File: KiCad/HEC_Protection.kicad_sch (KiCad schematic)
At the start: 19 parts, among them U10 74LS32, U11 74LS00, U11 74LS32, U12 74LS04, U17 74LS74, U18 74LS138, U18 74LS74, U19 74LS30, U22 74LS02, U23 74LS74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

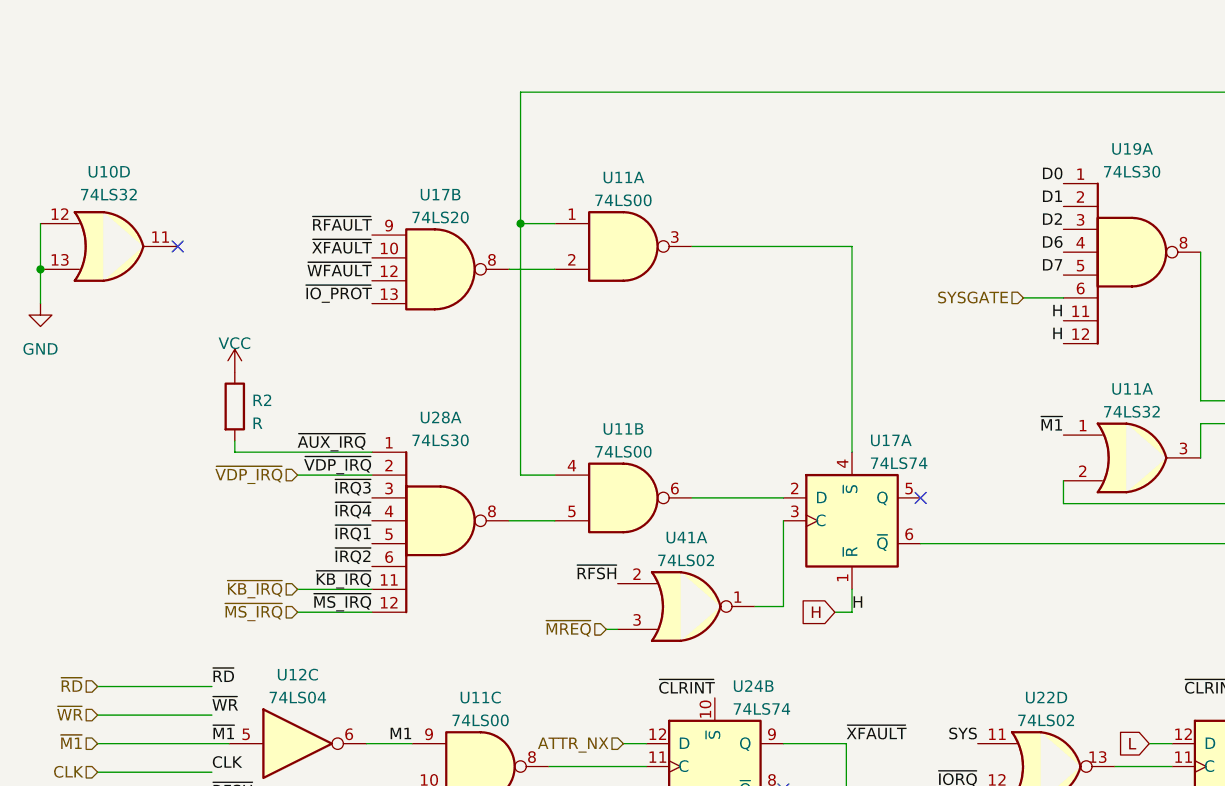
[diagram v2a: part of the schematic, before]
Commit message: New bus symbol
Updated bus symbol and footprint to simplify PCB layout.
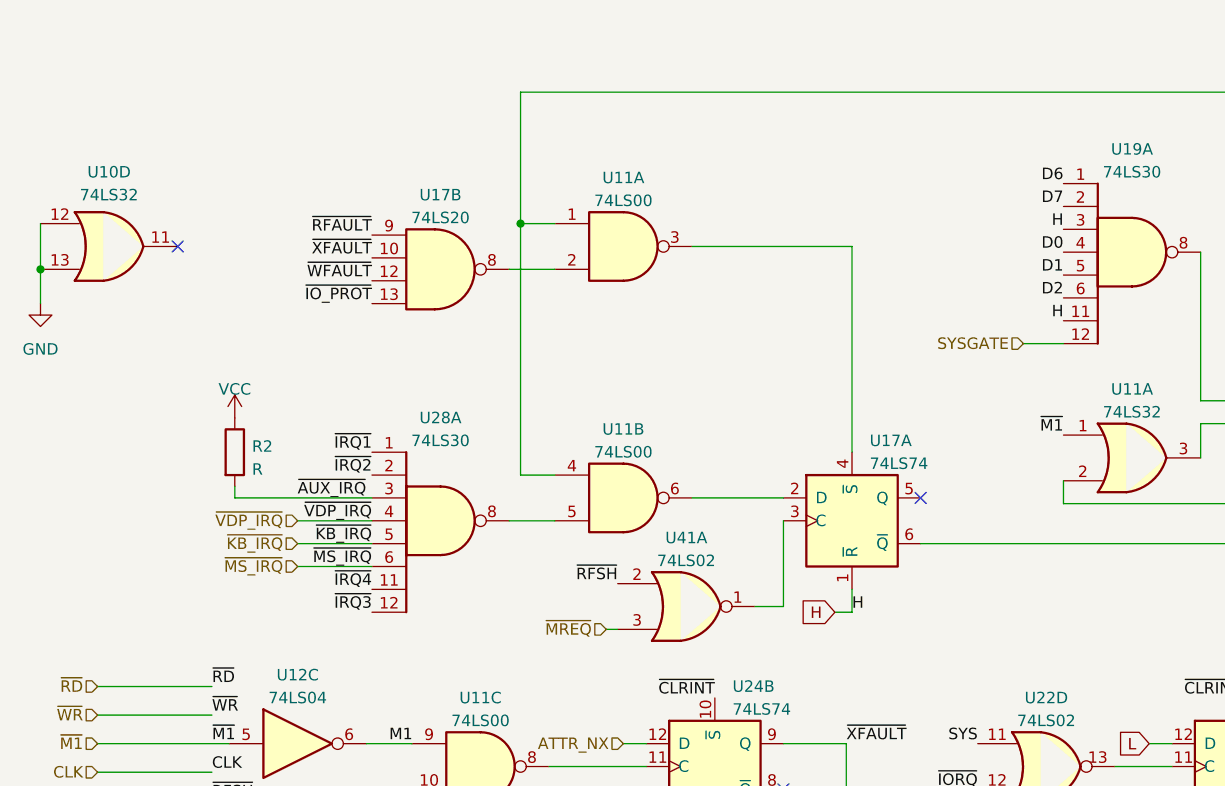
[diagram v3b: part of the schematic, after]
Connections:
- net D0: now also U19.4; no longer U19.1
- net D1: now also U19.5; no longer U19.2
- net D2: now also U19.6; no longer U19.3
- net D6: now also U19.1; no longer U19.4
- net D7: now also U19.2; no longer U19.5
- net H: now also U19.3; no longer U19.12
- net SYSGATE: now also U19.12; no longer U19.6
- net ~{AUX_IRQ}: now also U28.3; no longer U28.1
- net ~{IRQ1}: now also U28.1; no longer U28.5
- net ~{IRQ2}: now also U28.2; no longer U28.6
- net ~{IRQ3}: now also U28.12; no longer U28.3
- net ~{IRQ4}: now also U28.11; no longer U28.4
- net ~{KB_IRQ}: now also U28.5; no longer U28.11
- net ~{MS_IRQ}: now also U28.6; no longer U28.12
- net ~{VDP_IRQ}: now also U28.4; no longer U28.2
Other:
- moved on the sheet: R2
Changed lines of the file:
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@@
     (stroke (width 0) (type default))
   )
-  (wire (pts (xy 133.985 41.91) (xy 138.43 41.91))
-    (stroke (width 0) (type default))
-  )
-  (wire (pts (xy 53.34 76.835) (xy 61.595 76.835))
+  (wire (pts (xy 133.985 46.99) (xy 138.43 46.99))
+    (stroke (width 0) (type default))
+  )
+  (wire (pts (xy 53.34 71.755) (xy 61.595 71.755))
     (stroke (width 0) (type default))
   )
@@
     (stroke (width 0) (type default))
   )
-  (wire (pts (xy 46.355 57.785) (xy 46.355 59.055))
+  (wire (pts (xy 46.355 62.865) (xy 46.355 64.135))
     (stroke (width 0) (type default))
   )
@@
     (stroke (width 0) (type default))
   )
-  (wire (pts (xy 53.34 61.595) (xy 61.595 61.595))
+  (wire (pts (xy 53.34 66.675) (xy 61.595 66.675))
     (stroke (width 0) (type default))
   )
@@
     (stroke (width 0) (type default))
   )
-  (wire (pts (xy 46.355 59.055) (xy 61.595 59.055))
+  (wire (pts (xy 46.355 64.135) (xy 61.595 64.135))
     (stroke (width 0) (type default))
   )
@@
     (stroke (width 0) (type default))
   )
-  (wire (pts (xy 53.34 74.295) (xy 61.595 74.295))
+  (wire (pts (xy 53.34 69.215) (xy 61.595 69.215))
     (stroke (width 0) (type default))
   )
@@
     (effects (font (size 1.27 1.27)) (justify right bottom))
   )
-  (label "~{IRQ2}" (at 61.595 71.755 180) (fields_autoplaced)
+  (label "~{IRQ2}" (at 61.595 61.595 180) (fields_autoplaced)
     (effects (font (size 1.27 1.27)) (justify right bottom))
   )
@@
     (effects (font (size 1.27 1.27)) (justify left bottom))
   )
-  (label "D1" (at 138.43 31.75 180) (fields_autoplaced)
-    (effects (font (size 1.27 1.27)) (justify right bottom))
-  )
-  (label "~{VDP_IRQ}" (at 61.595 61.595 180) (fields_autoplaced)
+  (label "D1" (at 138.43 39.37 180) (fields_autoplaced)
+    (effects (font (size 1.27 1.27)) (justify right bottom))
+  )
+  (label "~{VDP_IRQ}" (at 61.595 66.675 180) (fields_autoplaced)
     (effects (font (size 1.27 1.27)) (justify right bottom))
   )
@@
     (effects (font (size 1.27 1.27)) (justify left bottom))
   )
-  (label "D0" (at 138.43 29.21 180) (fields_autoplaced)
+  (label "D0" (at 138.43 36.83 180) (fields_autoplaced)
     (effects (font (size 1.27 1.27)) (justify right bottom))
   )
@@
     (effects (font (size 1.27 1.27)) (justify left bottom))
   )
-  (label "~{IRQ3}" (at 61.595 64.135 180) (fields_autoplaced)
+  (label "~{IRQ3}" (at 61.595 76.835 180) (fields_autoplaced)
     (effects (font (size 1.27 1.27)) (justify right bottom))
   )
@@
     (effects (font (size 1.27 1.27)) (justify left bottom))
   )
-  (label "H" (at 138.43 46.99 180) (fields_autoplaced)
+  (label "H" (at 138.43 34.29 180) (fields_autoplaced)
     (effects (font (size 1.27 1.27)) (justify right bottom))
   )
@@
     (effects (font (size 1.27 1.27)) (justify left bottom))
   )
-  (label "D2" (at 138.43 34.29 180) (fields_autoplaced)
+  (label "D2" (at 138.43 41.91 180) (fields_autoplaced)
     (effects (font (size 1.27 1.27)) (justify right bottom))
   )
@@
     (effects (font (size 1.27 1.27)) (justify right bottom))
   )
-  (label "~{AUX_IRQ}" (at 60.96 59.055 180) (fields_autoplaced)
+  (label "~{AUX_IRQ}" (at 60.96 64.135 180) (fields_autoplaced)
     (effects (font (size 1.27 1.27)) (justify right bottom))
   )
@@
     (effects (font (size 1.27 1.27)) (justify right bottom))
   )
-  (label "D7" (at 138.43 39.37 180) (fields_autoplaced)
+  (label "D7" (at 138.43 31.75 180) (fields_autoplaced)
     (effects (font (size 1.27 1.27)) (justify right bottom))
   )
@@
     (effects (font (size 1.27 1.27)) (justify left bottom))
   )
-  (label "~{KB_IRQ}" (at 61.595 74.295 180) (fields_autoplaced)
+  (label "~{KB_IRQ}" (at 61.595 69.215 180) (fields_autoplaced)
     (effects (font (size 1.27 1.27)) (justify right bottom))
   )
@@
     (effects (font (size 1.27 1.27)) (justify right bottom))
   )
-  (label "D6" (at 138.43 36.83 180) (fields_autoplaced)
+  (label "D6" (at 138.43 29.21 180) (fields_autoplaced)
     (effects (font (size 1.27 1.27)) (justify right bottom))
   )
@@
     (effects (font (size 1.27 1.27)) (justify right bottom))
   )
-  (label "~{IRQ1}" (at 61.595 69.215 180) (fields_autoplaced)
+  (label "~{IRQ1}" (at 61.595 59.055 180) (fields_autoplaced)
     (effects (font (size 1.27 1.27)) (justify right bottom))
   )
@@
     (effects (font (size 1.27 1.27)) (justify right bottom))
   )
-  (label "~{MS_IRQ}" (at 61.595 76.835 180) (fields_autoplaced)
+  (label "~{MS_IRQ}" (at 61.595 71.755 180) (fields_autoplaced)
     (effects (font (size 1.27 1.27)) (justify right bottom))
   )
@@
     (effects (font (size 1.27 1.27)) (justify left bottom))
   )
-  (label "~{IRQ4}" (at 61.595 66.675 180) (fields_autoplaced)
+  (label "~{IRQ4}" (at 61.595 74.295 180) (fields_autoplaced)
     (effects (font (size 1.27 1.27)) (justify right bottom))
   )
@@
     (effects (font (size 1.27 1.27)) (justify right))
   )
-  (hierarchical_label "~{KB_IRQ}" (shape input) (at 53.34 74.295 180) (fields_autoplaced)
+  (hierarchical_label "~{KB_IRQ}" (shape input) (at 53.34 69.215 180) (fields_autoplaced)
     (effects (font (size 1.27 1.27)) (justify right))
   )
@@
     (effects (font (size 1.27 1.27)) (justify right))
   )
-  (hierarchical_label "SYSGATE" (shape input) (at 133.985 41.91 180) (fields_autoplaced)
+  (hierarchical_label "SYSGATE" (shape input) (at 133.985 46.99 180) (fields_autoplaced)
     (effects (font (size 1.27 1.27)) (justify right))
   )
@@
     (effects (font (size 1.27 1.27)) (justify left))
   )
-  (hierarchical_label "~{VDP_IRQ}" (shape input) (at 53.34 61.595 180) (fields_autoplaced)
+  (hierarchical_label "~{VDP_IRQ}" (shape input) (at 53.34 66.675 180) (fields_autoplaced)
     (effects (font (size 1.27 1.27)) (justify right))
   )
-  (hierarchical_label "~{MS_IRQ}" (shape input) (at 53.34 76.835 180) (fields_autoplaced)
+  (hierarchical_label "~{MS_IRQ}" (shape input) (at 53.34 71.755 180) (fields_autoplaced)
     (effects (font (size 1.27 1.27)) (justify right))
   )
@@
     )
   )
-  (symbol (lib_id "power:VCC") (at 46.355 50.165 0) (unit 1)
-    (in_bom yes) (on_board yes) (dnp no) (fields_autoplaced)
-    (property "Reference" "#PWR0111" (at 46.355 53.975 0)
-      (effects (font (size 1.27 1.27)) hide)
-    )
-    (property "Value" "VCC" (at 46.355 46.99 0)
-      (effects (font (size 1.27 1.27)))
-    )
-    (property "Footprint" "" (at 46.355 50.165 0)
-      (effects (font (size 1.27 1.27)) hide)
-    )
-    (property "Datasheet" "" (at 46.355 50.165 0)
+  (symbol (lib_id "power:VCC") (at 46.355 55.245 0) (unit 1)
+    (in_bom yes) (on_board yes) (dnp no) (fields_autoplaced)
+    (property "Reference" "#PWR0111" (at 46.355 59.055 0)
+      (effects (font (size 1.27 1.27)) hide)
+    )
+    (property "Value" "VCC" (at 46.355 52.07 0)
+      (effects (font (size 1.27 1.27)))
+    )
+    (property "Footprint" "" (at 46.355 55.245 0)
+      (effects (font (size 1.27 1.27)) hide)
+    )
+    (property "Datasheet" "" (at 46.355 55.245 0)
       (effects (font (size 1.27 1.27)) hide)
     )
@@
     )
   )
-  (symbol (lib_id "Device:R") (at 46.355 53.975 0) (unit 1)
-    (in_bom yes) (on_board yes) (dnp no) (fields_autoplaced)
-    (property "Reference" "R2" (at 48.26 53.34 0)
-      (effects (font (size 1.27 1.27)) (justify left))
-    )
-    (property "Value" "R" (at 48.26 55.88 0)
-      (effects (font (size 1.27 1.27)) (justify left))
-    )
-    (property "Footprint" "Resistor_THT:R_Axial_DIN0207_L6.3mm_D2.5mm_P7.62mm_Horizontal" (at 44.577 53.975 90)
-      (effects (font (size 1.27 1.27)) hide)
-    )
-    (property "Datasheet" "~" (at 46.355 53.975 0)
-      (effects (font (size 1.27 1.27)) hide)
-    )
+  (symbol (lib_id "Device:R") (at 46.355 59.055 0) (unit 1)
+    (in_bom yes) (on_board yes) (dnp no) (fields_autoplaced)
+    (property "Reference" "R2" (at 48.26 58.42 0)
+      (effects (font (size 1.27 1.27)) (justify left))
+    )
+    (property "Value" "R" (at 48.26 60.96 0)
+      (effects (font (size 1.27 1.27)) (justify left))
+    )
+    (property "Footprint" "Resistor_THT:R_Axial_DIN0207_L6.3mm_D2.5mm_P7.62mm_Horizontal" (at 44.577 59.055 90)
+      (effects (font (size 1.27 1.27)) hide)
+    )
+    (property "Datasheet" "~" (at 46.355 59.055 0)
+      (effects (font (size 1.27 1.27)) hide)
+    )

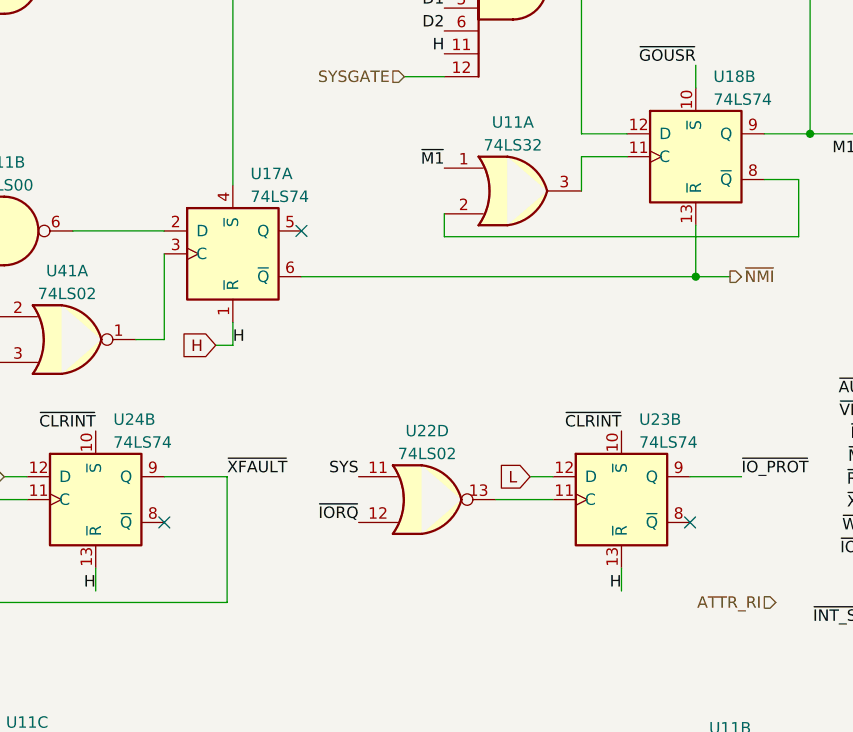
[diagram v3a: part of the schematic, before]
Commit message: Livestream routing
First routing livestream! Routed a data bus and some traces protection and memory region.
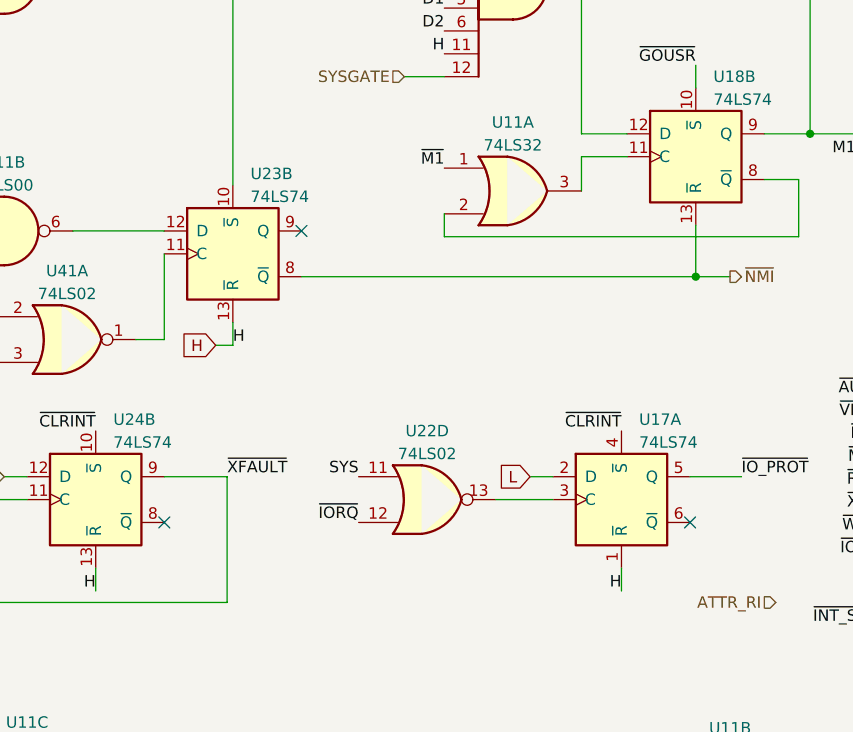
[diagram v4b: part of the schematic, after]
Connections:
- net L: now also U17.2 (D); no longer U23.12 (D)
- net ~{CLRINT}: now also U17.4 (~{S}); no longer U23.10 (~{S})
- net ~{IO_PROT}: now also U17.5 (Q); no longer U23.9 (Q)
- net ~{NMI}: now also U23.8 (~{Q}); no longer U17.6 (~{Q})
- net at U23.11 (C): now also U41.1; no longer U22.13
- net at U11.3: now also U23.10 (~{S}); no longer U17.4 (~{S})
- net at U17.3 (C): now also U22.13; no longer U41.1
- net at U11.6: now also U23.12 (D); no longer U17.2 (D)
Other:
- moved on the sheet: U17A, U23B
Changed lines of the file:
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@@
     )
   )
-  (symbol (lib_id "74xx:74LS74") (at 158.115 93.98 0) (unit 2)
-    (in_bom yes) (on_board yes) (dnp no) (fields_autoplaced)
-    (property "Reference" "U23" (at 160.0709 85.09 0)
-      (effects (font (size 1.27 1.27)) (justify left))
-    )
-    (property "Value" "74LS74" (at 160.0709 87.63 0)
-      (effects (font (size 1.27 1.27)) (justify left))
-    )
-    (property "Footprint" "Package_DIP:DIP-14_W7.62mm_Socket" (at 158.115 93.98 0)
-      (effects (font (size 1.27 1.27)) hide)
-    )
-    (property "Datasheet" "74xx/74hc_hct74.pdf" (at 158.115 93.98 0)
+  (symbol (lib_id "74xx:74LS74") (at 114.935 66.675 0) (unit 2)
+    (in_bom yes) (on_board yes) (dnp no) (fields_autoplaced)
+    (property "Reference" "U23" (at 116.8909 57.785 0)
+      (effects (font (size 1.27 1.27)) (justify left))
+    )
+    (property "Value" "74LS74" (at 116.8909 60.325 0)
+      (effects (font (size 1.27 1.27)) (justify left))
+    )
+    (property "Footprint" "Package_DIP:DIP-14_W7.62mm_Socket" (at 114.935 66.675 0)
+      (effects (font (size 1.27 1.27)) hide)
+    )
+    (property "Datasheet" "74xx/74hc_hct74.pdf" (at 114.935 66.675 0)
       (effects (font (size 1.27 1.27)) hide)
     )
@@
     )
   )
-  (symbol (lib_id "74xx:74LS74") (at 114.935 66.675 0) (unit 1)
-    (in_bom yes) (on_board yes) (dnp no) (fields_autoplaced)
-    (property "Reference" "U17" (at 116.8909 57.785 0)
-      (effects (font (size 1.27 1.27)) (justify left))
-    )
-    (property "Value" "74LS74" (at 116.8909 60.325 0)
-      (effects (font (size 1.27 1.27)) (justify left))
-    )
-    (property "Footprint" "Package_DIP:DIP-14_W7.62mm_Socket" (at 114.935 66.675 0)
-      (effects (font (size 1.27 1.27)) hide)
-    )
-    (property "Datasheet" "74xx/74hc_hct74.pdf" (at 114.935 66.675 0)
-      (effects (font (size 1.27 1.27)) hide)
-    )
+  (symbol (lib_id "74xx:74LS74") (at 158.115 93.98 0) (unit 1)
+    (in_bom yes) (on_board yes) (dnp no) (fields_autoplaced)
+    (property "Reference" "U17" (at 160.0709 85.09 0)
+      (effects (font (size 1.27 1.27)) (justify left))
+    )
+    (property "Value" "74LS74" (at 160.0709 87.63 0)
+      (effects (font (size 1.27 1.27)) (justify left))
+    )
+    (property "Footprint" "Package_DIP:DIP-14_W7.62mm_Socket" (at 158.115 93.98 0)
+      (effects (font (size 1.27 1.27)) hide)
+    )
+    (property "Datasheet" "74xx/74hc_hct74.pdf" (at 158.115 93.98 0)
+      (effects (font (size 1.27 1.27)) hide)
+    )

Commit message: Bug fixes
fixed some bugs introduced to the schematic. More routing.
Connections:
- net ATTR_RI: now also U11.4
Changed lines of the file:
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@@
     (effects (font (size 1.27 1.27)) (justify right))
   )
-  (hierarchical_label "ATTR_RI" (shape input) (at 175.26 105.41 180) (fields_autoplaced)
+  (hierarchical_label "ATTR_RI" (shape input) (at 159.385 124.46 180) (fields_autoplaced)
     (effects (font (size 1.27 1.27)) (justify right))
   )

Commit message: Livestream commit
Committing live! Just to make sure that I don't lose 1 day of work.
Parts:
- added unit 4 of U41
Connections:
- net GND: now also U12.5, U41.11; no longer U10.12, U10.13
- net M1: now also U11.12, U41.13; no longer U11.9, U12.6
- net VCC: now also U10.12, U10.13
- net ~{M1}: now also U41.12; no longer U12.5
- net ~{RFAULT}: now also U17.10; no longer U17.9
- net ~{WFAULT}: now also U11.10; no longer U11.13
- net ~{WR}: now also U11.9; no longer U11.12
- net ~{XFAULT}: now also U11.13, U17.9; no longer U11.10, U17.10
- net at U11.8: now also U24.3 (C); no longer U24.11 (C)
- net at U11.11: now also U24.11 (C); no longer U24.3 (C)
- no-connect marks 14 -> 15
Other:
- moved on the sheet: U11C, U11D, U12C
